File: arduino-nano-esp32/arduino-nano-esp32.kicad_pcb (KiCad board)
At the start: 2 copper layers, 61 x 48.3 mm, 4 parts

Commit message: cleanup
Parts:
- removed the REF** at (116.8, 111.8)
- added A1: Arduino_Nano_ESP32_Socket, PCM_arduino-library:Arduino_Nano_ESP32_Socket, F.Cu at (109.2, 72.4)
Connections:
- REF** pad 1: (no net) -> GND
- REF** pad 2: (no net) -> GND
- REF** pad 8: (no net) -> GND
- REF** pad 9: (no net) -> +3.3V
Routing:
- net (no net): track 242.0 -> 0.00 mm
- net unconnected-(A1-PadB1): track 0.00 -> 33.6 mm
- net unconnected-(A1-PadD7): track 0.00 -> 17.3 mm
- net unconnected-(A1-PadD8): track 0.00 -> 17.3 mm
- net unconnected-(A1-PadD6): track 0.00 -> 17.3 mm
- net unconnected-(A1-PadD5): track 0.00 -> 17.3 mm
- net unconnected-(A1-PadD4): track 0.00 -> 17.3 mm
- net unconnected-(A1-PadD3): track 0.00 -> 17.3 mm
- net unconnected-(A1-PadD2): track 0.00 -> 16.3 mm
- added copper zone on F.Cu, net +3.3V
- added copper zone on B.Cu, net GND

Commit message: symbol lib
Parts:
- removed REF** (x2): 3x4 switch, maciek-lib:3x4 switch
- removed REF**: lora-adafruit, maciek-lib:lora-adafruit
- added RFM95W1: ~, maciek-lib:lora-adafruit, F.Cu at (144.8, 83.8)
- added SW1: ~, maciek-lib:3x4 switch, F.Cu at (135.9, 111.8)
- added SW2: ~, maciek-lib:3x4 switch, F.Cu at (135.9, 101.6)
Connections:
- A1 pad B1: unconnected-(A1-PadB1) -> Net-(A1-PadB1)
- A1 pad D2: unconnected-(A1-PadD2) -> Net-(A1-PadD2)
- A1 pad D3: unconnected-(A1-PadD3) -> Net-(A1-PadD3)
- A1 pad D4: unconnected-(A1-PadD4) -> Net-(A1-PadD4)
- A1 pad D5: unconnected-(A1-PadD5) -> Net-(A1-PadD5)
- A1 pad D6: unconnected-(A1-PadD6) -> Net-(A1-PadD6)
- A1 pad D7: unconnected-(A1-PadD7) -> Net-(A1-PadD7)
- A1 pad D8: unconnected-(A1-PadD8) -> Net-(A1-PadD8)
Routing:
- net unconnected-(A1-PadB1): track 33.6 -> 0.00 mm
- net Net-(A1-PadB1): track 0.00 -> 33.6 mm
- net unconnected-(A1-PadD7): track 17.3 -> 0.00 mm
- net Net-(A1-PadD7): track 0.00 -> 17.3 mm
- net unconnected-(A1-PadD8): track 17.3 -> 0.00 mm
- net unconnected-(A1-PadD6): track 17.3 -> 0.00 mm
- net unconnected-(A1-PadD5): track 17.3 -> 0.00 mm
- net unconnected-(A1-PadD4): track 17.3 -> 0.00 mm
- net unconnected-(A1-PadD3): track 17.3 -> 0.00 mm
- net Net-(A1-PadD8): track 0.00 -> 17.3 mm
- net Net-(A1-PadD6): track 0.00 -> 17.3 mm
- net Net-(A1-PadD5): track 0.00 -> 17.3 mm
- net Net-(A1-PadD4): track 0.00 -> 17.3 mm
- net Net-(A1-PadD3): track 0.00 -> 17.3 mm
- net unconnected-(A1-PadD2): track 16.3 -> 0.00 mm
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
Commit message: gen gerbers
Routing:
- net Net-(A1-PadB1): track 33.6 -> 35.7 mm
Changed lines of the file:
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@@
 	(segment
 		(start 104.14 106.68)
-		(end 111.76 114.3)
+		(end 114.3 116.84)
 		(width 0.2)
 		(layer "F.Cu")
@@
 	)
 	(segment
-		(start 111.76 114.3)
+		(start 129.54 116.84)
 		(end 132.08 114.3)
 		(width 0.2)
@@
 		(width 0.2)
 		(layer "F.Cu")
+		(net 24)
+	)
+	(segment
+		(start 114.3 116.84)
+		(end 129.54 116.84)
+		(width 0.2)
+		(layer "F.Cu")

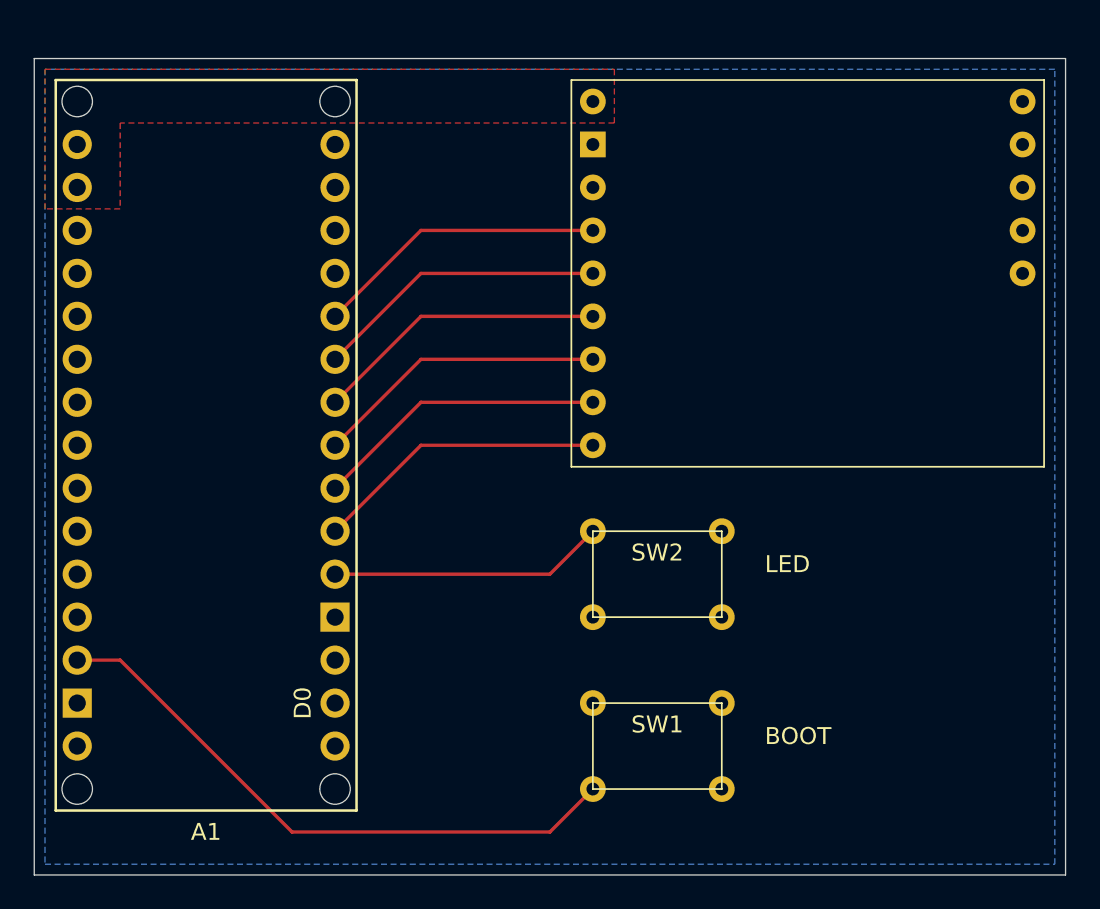
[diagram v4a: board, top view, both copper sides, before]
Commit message: add nests and 3v3 area
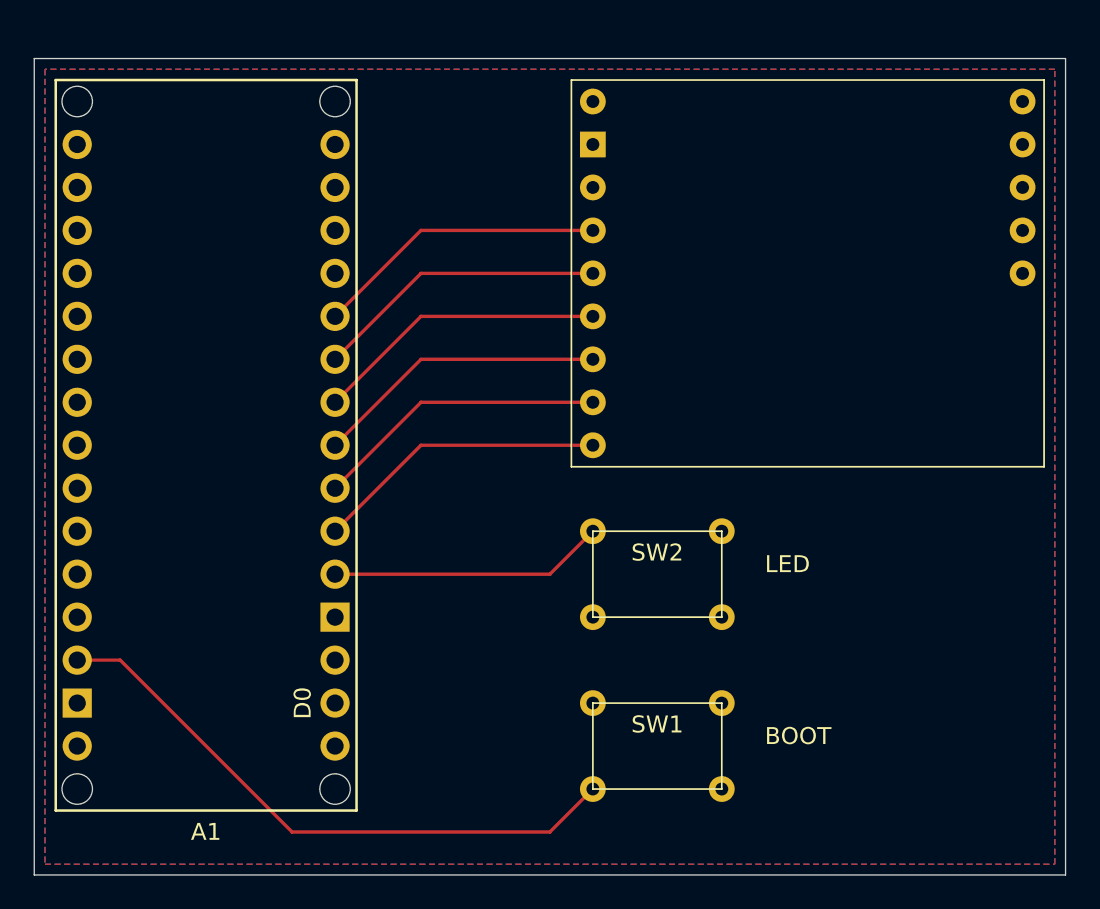
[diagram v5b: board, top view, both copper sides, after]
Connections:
- net Net-(RFM95W1-CS) renamed /CS
- net Net-(RFM95W1-G0) renamed /G0
- net Net-(RFM95W1-MISO) renamed /MISO
- net Net-(RFM95W1-MOSI) renamed /MOSI
- net Net-(RFM95W1-RST) renamed /RST
- net Net-(RFM95W1-SCK) renamed /SCK
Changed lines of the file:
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@@
 	(net 26 "unconnected-(SW2-Pad4)")
 	(net 27 "unconnected-(SW2-Pad3)")
-	(net 28 "Net-(RFM95W1-G0)")
-	(net 29 "Net-(RFM95W1-RST)")
-	(net 30 "Net-(RFM95W1-SCK)")
-	(net 31 "Net-(RFM95W1-CS)")
-	(net 32 "Net-(RFM95W1-MOSI)")
-	(net 33 "Net-(RFM95W1-MISO)")
-	(net 34 "unconnected-(RFM95W1-G4-Pad11)")
-	(net 35 "unconnected-(RFM95W1-G5-Pad10)")
-	(net 36 "unconnected-(RFM95W1-EN-Pad7)")
-	(net 37 "unconnected-(RFM95W1-G1-Pad14)")
-	(net 38 "unconnected-(RFM95W1-G2-Pad13)")
-	(net 39 "unconnected-(RFM95W1-G3-Pad12)")
+	(net 28 "unconnected-(RFM95W1-G4-Pad11)")
+	(net 29 "unconnected-(RFM95W1-G5-Pad10)")
+	(net 30 "unconnected-(RFM95W1-EN-Pad7)")
+	(net 31 "unconnected-(RFM95W1-G1-Pad14)")
+	(net 32 "unconnected-(RFM95W1-G2-Pad13)")
+	(net 33 "unconnected-(RFM95W1-G3-Pad12)")
+	(net 34 "/SCK")
+	(net 35 "/MISO")
+	(net 36 "/CS")
+	(net 37 "/RST")
+	(net 38 "/MOSI")
+	(net 39 "/G0")
 	(footprint "maciek-lib:lora-adafruit"
 		(layer "F.Cu")
@@
 			(layers "*.Cu" "*.Mask")
 			(remove_unused_layers no)
-			(net 29 "Net-(RFM95W1-RST)")
+			(net 37 "/RST")
 			(pinfunction "RST")
 			(pintype "input")
@@
 			(layers "*.Cu" "*.Mask")
 			(remove_unused_layers no)
-			(net 31 "Net-(RFM95W1-CS)")
+			(net 36 "/CS")
 			(pinfunction "CS")
 			(pintype "input")
@@
 			(layers "*.Cu" "*.Mask")
 			(remove_unused_layers no)
-			(net 32 "Net-(RFM95W1-MOSI)")
+			(net 38 "/MOSI")
 			(pinfunction "MOSI")
 			(pintype "input")
@@
 			(layers "*.Cu" "*.Mask")
 			(remove_unused_layers no)
-			(net 33 "Net-(RFM95W1-MISO)")
+			(net 35 "/MISO")
 			(pinfunction "MISO")
 			(pintype "input")
@@
 			(layers "*.Cu" "*.Mask")
 			(remove_unused_layers no)
-			(net 30 "Net-(RFM95W1-SCK)")
+			(net 34 "/SCK")
 			(pinfunction "SCK")
 			(pintype "input")
@@
 			(layers "*.Cu" "*.Mask")
 			(remove_unused_layers no)
-			(net 28 "Net-(RFM95W1-G0)")
+			(net 39 "/G0")
 			(pinfunction "G0")
 			(pintype "input")
@@
 			(layers "*.Cu" "*.Mask")
 			(remove_unused_layers no)
-			(net 36 "unconnected-(RFM95W1-EN-Pad7)")
+			(net 30 "unconnected-(RFM95W1-EN-Pad7)")
 			(pinfunction "EN")
 			(pintype "input+no_connect")
@@
 			(layers "*.Cu" "*.Mask")
 			(remove_unused_layers no)
-			(net 35 "unconnected-(RFM95W1-G5-Pad10)")
+			(net 29 "unconnected-(RFM95W1-G5-Pad10)")
 			(pinfunction "G5")
 			(pintype "input+no_connect")
@@
 			(layers "*.Cu" "*.Mask")
 			(remove_unused_layers no)
-			(net 34 "unconnected-(RFM95W1-G4-Pad11)")
+			(net 28 "unconnected-(RFM95W1-G4-Pad11)")
 			(pinfunction "G4")
 			(pintype "input+no_connect")
@@
 			(layers "*.Cu" "*.Mask")
 			(remove_unused_layers no)
-			(net 39 "unconnected-(RFM95W1-G3-Pad12)")
+			(net 33 "unconnected-(RFM95W1-G3-Pad12)")
 			(pinfunction "G3")
 			(pintype "input+no_connect")
@@
 			(layers "*.Cu" "*.Mask")
 			(remove_unused_layers no)
-			(net 38 "unconnected-(RFM95W1-G2-Pad13)")
+			(net 32 "unconnected-(RFM95W1-G2-Pad13)")
 			(pinfunction "G2")
 			(pintype "input+no_connect")
@@
 			(layers "*.Cu" "*.Mask")
 			(remove_unused_layers no)
-			(net 37 "unconnected-(RFM95W1-G1-Pad14)")
+			(net 31 "unconnected-(RFM95W1-G1-Pad14)")
 			(pinfunction "G1")
 			(pintype "input+no_connect")
@@
 			(layers "*.Cu" "*.Mask")
 			(remove_unused_layers no)
-			(net 29 "Net-(RFM95W1-RST)")
+			(net 37 "/RST")
 			(pinfunction "D3")
 			(pintype "bidirectional")
@@
 			(layers "*.Cu" "*.Mask")
 			(remove_unused_layers no)
-			(net 31 "Net-(RFM95W1-CS)")
+			(net 36 "/CS")
 			(pinfunction "D4")
 			(pintype "bidirectional")
@@
 			(layers "*.Cu" "*.Mask")
 			(remove_unused_layers no)
-			(net 32 "Net-(RFM95W1-MOSI)")
+			(net 38 "/MOSI")
 			(pinfunction "D5")
 			(pintype "bidirectional")
@@
 			(layers "*.Cu" "*.Mask")
 			(remove_unused_layers no)
-			(net 33 "Net-(RFM95W1-MISO)")
+			(net 35 "/MISO")
 			(pinfunction "D6")
 			(pintype "bidirectional")
@@
 			(layers "*.Cu" "*.Mask")
 			(remove_unused_layers no)
-			(net 30 "Net-(RFM95W1-SCK)")
+			(net 34 "/SCK")
 			(pinfunction "D7")
 			(pintype "bidirectional")
@@
 			(layers "*.Cu" "*.Mask")
 			(remove_unused_layers no)
-			(net 28 "Net-(RFM95W1-G0)")
+			(net 39 "/G0")
 			(pinfunction "D8")
 			(pintype "bidirectional")
@@
 	)
 	(segment
+		(start 121.92 83.82)
+		(end 132.08 83.82)
+		(width 0.2)
+		(layer "F.Cu")
+		(net 34)
+	)
+	(segment
+		(start 116.84 88.9)
+		(end 121.92 83.82)
+		(width 0.2)
+		(layer "F.Cu")
+		(net 34)
+	)
+	(segment
+		(start 116.84 91.44)
+		(end 121.92 86.36)
+		(width 0.2)
+		(layer "F.Cu")
+		(net 35)
+	)
+	(segment
+		(start 121.92 86.36)
+		(end 132.08 86.36)
+		(width 0.2)
+		(layer "F.Cu")
+		(net 35)
+	)
+	(segment
+		(start 116.84 96.52)
+		(end 121.92 91.44)
+		(width 0.2)
+		(layer "F.Cu")
+		(net 36)
+	)
+	(segment
+		(start 121.92 91.44)
+		(end 132.08 91.44)
+		(width 0.2)
+		(layer "F.Cu")
+		(net 36)
+	)
+	(segment
+		(start 116.84 99.06)
+		(end 121.92 93.98)
+		(width 0.2)
+		(layer "F.Cu")
+		(net 37)
+	)
+	(segment
+		(start 121.92 93.98)
+		(end 132.08 93.98)
+		(width 0.2)
+		(layer "F.Cu")
+		(net 37)
+	)
+	(segment
+		(start 116.84 93.98)
+		(end 121.92 88.9)
+		(width 0.2)
+		(layer "F.Cu")
+		(net 38)
+	)
+	(segment
+		(start 121.92 88.9)
+		(end 132.08 88.9)
+		(width 0.2)
+		(layer "F.Cu")
+		(net 38)
+	)
+	(segment
 		(start 132.08 81.28)
 		(end 121.92 81.28)
 		(width 0.2)
 		(layer "F.Cu")
-		(net 28)
+		(net 39)
 	)
 	(segment
@@
 		(width 0.2)
 		(layer "F.Cu")
-		(net 28)
-	)
-	(segment
-		(start 116.84 99.06)
-		(end 121.92 93.98)
-		(width 0.2)
-		(layer "F.Cu")
-		(net 29)
-	)
-	(segment
-		(start 121.92 93.98)
-		(end 132.08 93.98)
-		(width 0.2)
-		(layer "F.Cu")
-		(net 29)
-	)
-	(segment
-		(start 121.92 83.82)
-		(end 132.08 83.82)
-		(width 0.2)
-		(layer "F.Cu")
-		(net 30)
-	)
-	(segment
-		(start 116.84 88.9)
-		(end 121.92 83.82)
-		(width 0.2)
-		(layer "F.Cu")
-		(net 30)
-	)
-	(segment
-		(start 116.84 96.52)
-		(end 121.92 91.44)
-		(width 0.2)
-		(layer "F.Cu")
-		(net 31)
-	)
-	(segment
-		(start 121.92 91.44)
-		(end 132.08 91.44)
-		(width 0.2)
-		(layer "F.Cu")
-		(net 31)
-	)
-	(segment
-		(start 116.84 93.98)
-		(end 121.92 88.9)
-		(width 0.2)
-		(layer "F.Cu")
-		(net 32)
-	)
-	(segment
-		(start 121.92 88.9)
-		(end 132.08 88.9)
-		(width 0.2)
-		(layer "F.Cu")
-		(net 32)
-	)
-	(segment
-		(start 116.84 91.44)
-		(end 121.92 86.36)
-		(width 0.2)
-		(layer "F.Cu")
-		(net 33)
-	)
-	(segment
-		(start 121.92 86.36)
-		(end 132.08 86.36)
-		(width 0.2)
-		(layer "F.Cu")
-		(net 33)
+		(net 39)
 	)
 	(zone
@@
 		(polygon
 			(pts
-				(xy 99.695 80.01) (xy 99.695 71.755) (xy 133.35 71.755) (xy 133.35 74.93) (xy 104.14 74.93) (xy 104.14 80.01)
-			)
-		)
+				(xy 99.695 118.745) (xy 159.385 118.745) (xy 159.385 71.755) (xy 99.695 71.755)
+			)
+		)

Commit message: need bigger holes
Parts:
- added J1: Conn_01x02_Pin, Connector_PinHeader_2.54mm:PinHeader_1x02_P2.54mm_Horizontal, F.Cu at (127.0, 109.2)
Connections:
- A1 pad VIN: unconnected-(A1-PadVIN) -> +BATT
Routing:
- net +BATT: track 0.00 -> 29.6 mm
